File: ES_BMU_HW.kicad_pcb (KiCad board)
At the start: 2 copper layers, 100 x 100 mm, 84 parts, among them IC1 ADBMS6821CCSZ, J5 Conn_02x03_Top_Bottom, Q1 SQ2362CES, Q3 SQ2362CES, Q6 SQ2362CES, Q7 SQ2362CES, Q8 SQ2362CES, SW1 SW_Nidec_CAS-120A1, SW3 SW_Nidec_CAS-120A1, T1 74941301, U1 TPS542025, U15 SN65HVD234, U2 LM393, U3 STM32G474CETx, U4 SN65HVD234, U5 ADS1113IDGS, U7 TLV777, Y2 16 MHz

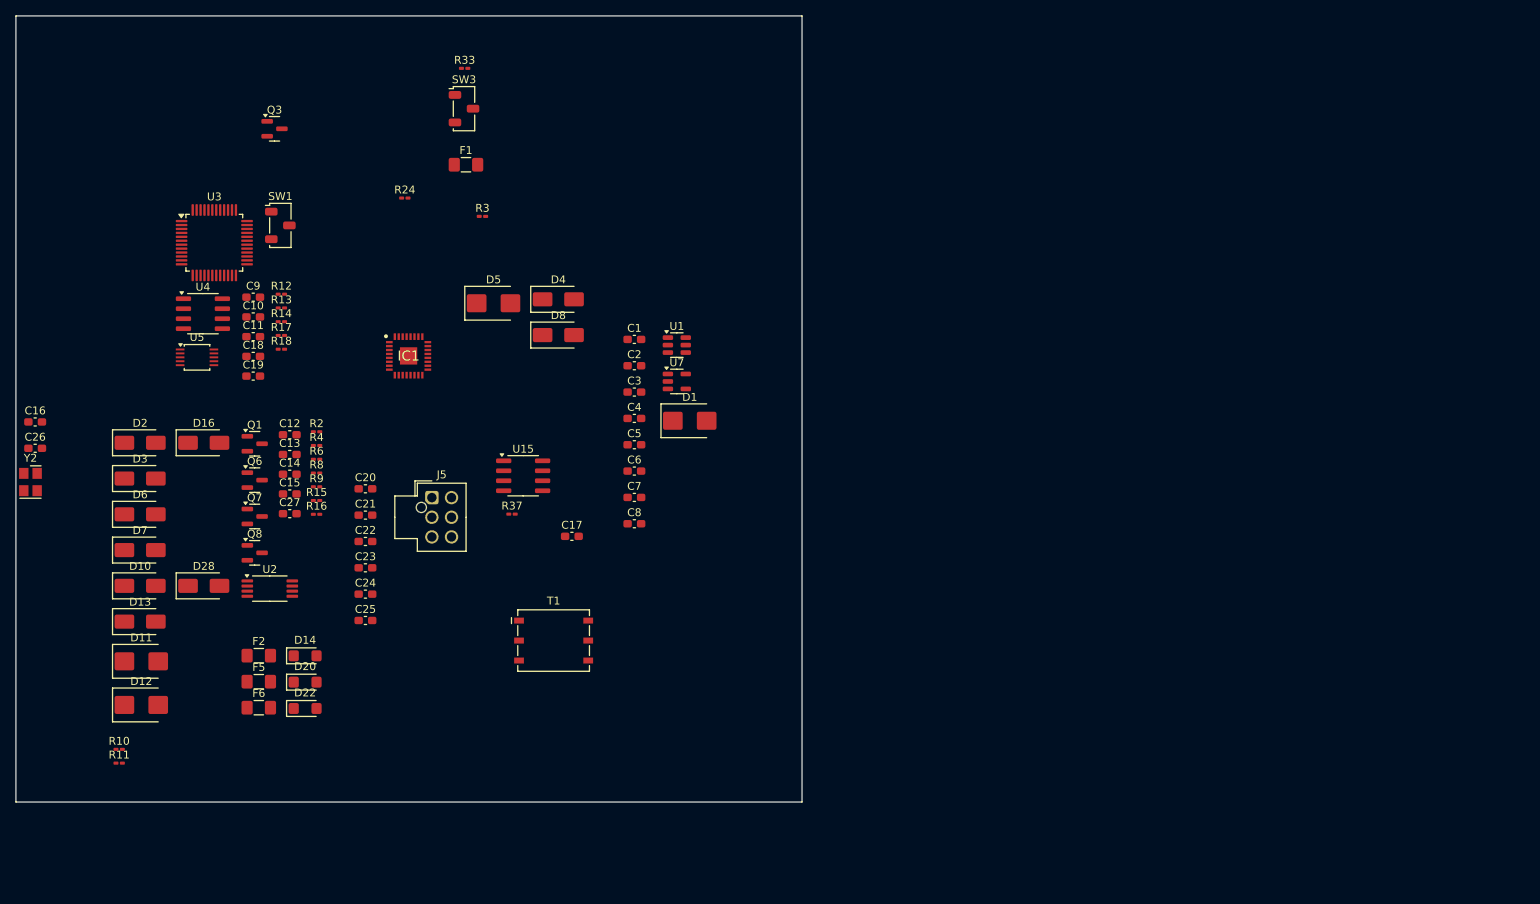
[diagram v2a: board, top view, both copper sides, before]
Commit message: - Primer placement dels components - Footprint afegit per la bobina - S'han tret els TVS a les entrades dels contactors auxiliars
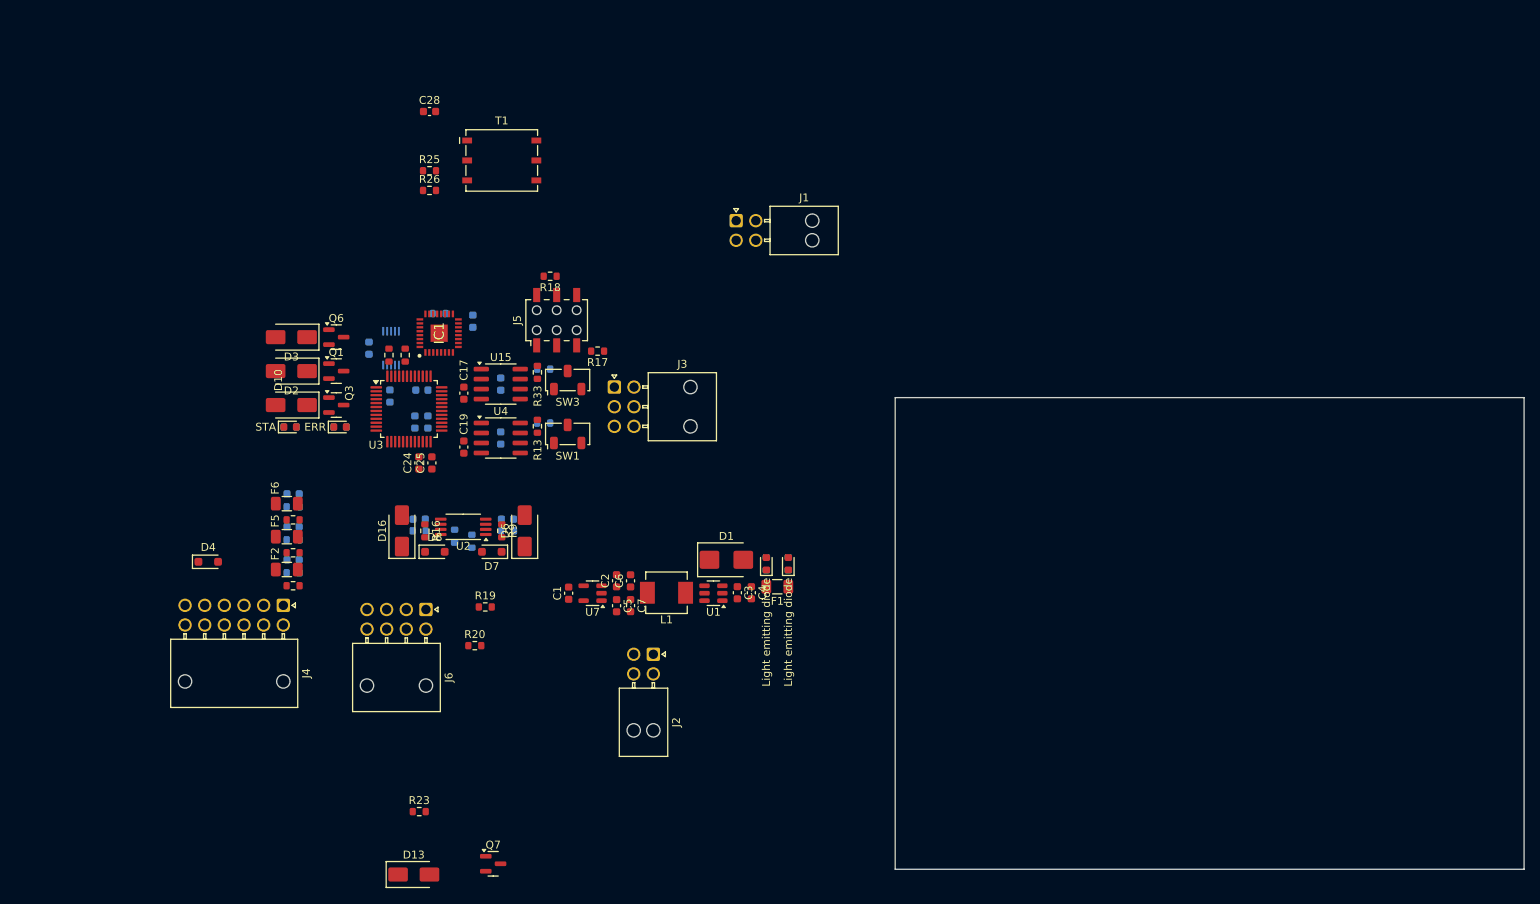
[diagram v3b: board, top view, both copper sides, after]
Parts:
- removed C16, C26: 22p, Capacitor_SMD:C_0603_1608Metric_Pad1.08x0.95mm_HandSolder
- removed D11, D12, D5: SMBJ3V3, Diode_SMD:D_SMB
- removed D20, D22: AR1FJ, Diode_SMD:D_SMF
- removed D28: SMAJ30A, Diode_SMD:D_SMA
- removed Q8: SQ2362CES, Package_TO_SOT_SMD:SOT-23
- removed R10, R11: 2k2, Resistor_SMD:R_0201_0603Metric_Pad0.64x0.40mm_HandSolder
- removed Y2: 16 MHz, Crystal_SMD_Wurth:Y_Wurth_WE-XTAL_Quartz-CFPX-180
- added C28: 1u, Capacitor_SMD:C_0603_1608Metric, F.Cu at (116.4, 51.6)
- added D15: LED, LED_SMD:LED_0603_1608Metric, F.Cu at (162.1, 109.1)
- added D17: LED, LED_SMD:LED_0603_1608Metric, F.Cu at (159.3, 109.1)
- added D9: LED, LED_SMD:LED_0603_1608Metric, F.Cu at (105.0, 91.7)
- added J1: Conn_02x02_Counter_Clockwise, Connector_Molex:Molex_Nano-Fit_105314-xx04_2x02_P2.50mm_Horizontal, F.Cu at (155.4, 65.4)
- added J2: Conn_02x02_Counter_Clockwise, Connector_Molex:Molex_Nano-Fit_105314-xx04_2x02_P2.50mm_Horizontal, F.Cu at (144.9, 120.6)
- added J3: Conn_02x03_Top_Bottom, Connector_Molex:Molex_Nano-Fit_105314-xx06_2x03_P2.50mm_Horizontal, F.Cu at (139.9, 86.6)
- added J4: Conn_02x06_Top_Bottom, Connector_Molex:Molex_Nano-Fit_105314-xx12_2x06_P2.50mm_Horizontal, F.Cu at (97.8, 114.4)
- added J6: Conn_02x04_Top_Bottom, Connector_Molex:Molex_Nano-Fit_105314-xx08_2x04_P2.50mm_Horizontal, F.Cu at (116.0, 114.9)
- added L1: 15u, Inductor_SMD:L_Vishay_IHLP-2020, F.Cu at (146.6, 112.8)
- added R1: 100, Resistor_SMD:R_0603_1608Metric, F.Cu at (99.1, 111.9)
- added R19: 100k, Resistor_SMD:R_0603_1608Metric, F.Cu at (123.5, 114.6)
- added R20: 100k, Resistor_SMD:R_0603_1608Metric, F.Cu at (122.2, 119.5)
- added R21: 2k2, Resistor_SMD:R_0603_1608Metric, B.Cu at (105.0, 91.7)
- added R22: 2k2, Resistor_SMD:R_0603_1608Metric, B.Cu at (98.7, 91.7)
- added R23: 100k, Resistor_SMD:R_0603_1608Metric, F.Cu at (115.1, 140.6)
- added R25: 100k, Resistor_SMD:R_0603_1608Metric, F.Cu at (116.4, 59.1)
- added R26: 100k, Resistor_SMD:R_0603_1608Metric, F.Cu at (116.4, 61.6)
- added R27: 10k, Resistor_SMD:R_0603_1608Metric, F.Cu at (113.3, 82.5)
- added R28: 10k, Resistor_SMD:R_0603_1608Metric, F.Cu at (111.3, 82.5)
- added R29: 10k, Resistor_SMD:R_0603_1608Metric, B.Cu at (162.1, 109.1)
- added R30: 10k, Resistor_SMD:R_0603_1608Metric, B.Cu at (159.3, 109.1)
- added R5: 100, Resistor_SMD:R_0603_1608Metric, F.Cu at (99.1, 107.7)
- added R7: 100, Resistor_SMD:R_0603_1608Metric, F.Cu at (99.1, 103.5)
- C1, C17, C19, C2, C24, C25, C3, C4, C5, C6, C7: footprint Capacitor_SMD:C_0603_1608Metric_Pad1.08x0.95mm_HandSolder -> Capacitor_SMD:C_0603_1608Metric
- C10, C11, C18, C20, C21, C22, C23, C8, C9: footprint Capacitor_SMD:C_0603_1608Metric_Pad1.08x0.95mm_HandSolder -> Capacitor_SMD:C_0603_1608Metric; moved to B.Cu
- C12, C13, C14: value 10u -> 4u7; footprint Capacitor_SMD:C_0603_1608Metric_Pad1.08x0.95mm_HandSolder -> Capacitor_SMD:C_0603_1608Metric; moved to B.Cu
- C15, C27: value 100n -> 10n; footprint Capacitor_SMD:C_0603_1608Metric_Pad1.08x0.95mm_HandSolder -> Capacitor_SMD:C_0603_1608Metric; moved to B.Cu
- D14: value AR1FJ -> LED; footprint Diode_SMD:D_SMF -> LED_SMD:LED_0603_1608Metric
- D4, D7, D8: value D_Schottky -> SD103AWS-G3-18; footprint Diode_SMD:D_SMA -> Diode_SMD:D_SOD-323_HandSoldering
- F1, F2, F5, F6: footprint Fuse:Fuse_1206_3216Metric_Pad1.42x1.75mm_HandSolder -> Fuse:Fuse_1206_3216Metric
- J5: footprint Connector_Molex:Molex_Nano-Fit_105310-xx06_2x03_P2.50mm_Vertical -> Connector_Wuerth:Wuerth_WR-PHD_610006243021_SMD_2x03_P2.54mm_Vertical
- R12, R14, R3, R37, R4, R6: footprint Resistor_SMD:R_0201_0603Metric_Pad0.64x0.40mm_HandSolder -> Resistor_SMD:R_0603_1608Metric; moved to B.Cu
- R13, R16, R17, R18, R33, R9: footprint Resistor_SMD:R_0201_0603Metric_Pad0.64x0.40mm_HandSolder -> Resistor_SMD:R_0603_1608Metric
- R15, R8: value 470k -> 100k; footprint Resistor_SMD:R_0201_0603Metric_Pad0.64x0.40mm_HandSolder -> Resistor_SMD:R_0603_1608Metric; moved to B.Cu
- R2, R24: value 10k -> 100k; footprint Resistor_SMD:R_0201_0603Metric_Pad0.64x0.40mm_HandSolder -> Resistor_SMD:R_0603_1608Metric; moved to B.Cu
- U3: value STM32G474CETx -> STM32G474CBTx
- U5: moved to B.Cu
- moved F1 66.7 mm to (160.7, 112.0), turned to 180 degrees
- moved T1 61.4 mm to (125.6, 57.8)
- moved D4 55.7 mm to (88.3, 108.8)
- moved Q7 53.6 mm to (124.5, 147.3)
- moved R3 51.3 mm to (99.1, 110.2), turned to 180 degrees
- moved D6 49.0 mm to (128.5, 104.9), turned to 90 degrees
- moved D13 47.4 mm to (114.4, 148.6)
- moved SW1 45.2 mm to (134.0, 92.6), turned to 90 degrees
- moved D7 44.7 mm to (124.3, 107.6), turned to 180 degrees
- moved R24 43.5 mm to (119.6, 105.6), turned to 90 degrees
- moved U4 41.1 mm to (125.5, 93.1)
- moved R17 40.3 mm to (137.8, 82.0), turned to 180 degrees
- moved R33 39.8 mm to (130.1, 84.7), turned to -90 degrees
- moved SW3 37.0 mm to (134.0, 85.7), turned to 90 degrees
- moved Q3 36.0 mm to (104.6, 88.9)
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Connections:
- net /GPIO/AIR+Coil- renamed AIR+Coil-
- net /GPIO/AIR-Coil- renamed AIR-Coil-
- net /GPIO/ActiveButton renamed ActiveButton
- net /GPIO/BMSStateOutput renamed BMSerrorOutput
- net /GPIO/SDCinput renamed SDCinput
- net /stm32/CAN1H renamed CAN1H
- net /stm32/CAN1L renamed CAN1L
- net /stm32/CAN2H renamed CAN2H
- net /stm32/CAN2L renamed CAN2L
- C12 pad 1: /GPIO/AuxAIRpre -> AuxAIRpre
- C13 pad 1: /GPIO/AuxAIR- -> AuxAIR-
- C14 pad 1: /GPIO/AuxAIR+ -> AuxAIR+
- D10 pad 1: /GPIO/AIRpreCoil- -> AIRpreCoil-
- D14 pad 1: SDC -> GND
- D14 pad 2: /GPIO/AIRpreCoil- -> Net-(D14-A)
- D4 pad 1: /GPIO/PwrAuxAIR+ -> PwrAuxAIR
- F2 pad 2: /GPIO/RawAuxAIRpre -> RawAuxAIRpre
- F5 pad 2: /GPIO/RawAuxAIR- -> RawAuxAIR-
- F6 pad 2: /GPIO/RawAuxAIR+ -> RawAuxAIR+
- Q1 pad 1: /GPIO/ControlAIR- -> ControlAIR-
- Q3 pad 1: /GPIO/ControlAIRpre -> ControlAIRpre
- Q3 pad 3: /GPIO/AIRpreCoil- -> AIRpreCoil-
- Q6 pad 1: /GPIO/ControlAIR+ -> ControlAIR+
- Q7 pad 1: /GPIO/ControlBMSState -> BMSerror
- R2 pad 2: /GPIO/ActiveButtonState -> ActiveButtonState
- R24 pad 2: /GPIO/SDCendState -> SDCendState
- R3 pad 1: /GPIO/AuxAIRpre -> AuxAIRpre
- R4 pad 1: /GPIO/AuxAIR- -> AuxAIR-
- R6 pad 1: /GPIO/AuxAIR+ -> AuxAIR+
- T1 pad 1: /stm32/IPA -> isoIMA
- T1 pad 3: /stm32/IMA -> isoIPA
- T1 pad 4: /stm32/IMA_EXT -> /stm32/IPA
- T1 pad 6: /stm32/IPA_EXT -> /stm32/IMA
- U2 pad 1: /GPIO/ActiveButtonState -> ActiveButtonState
- U2 pad 7: /GPIO/SDCendState -> SDCendState
- U3 pad 10: /stm32/ControlAIRpre -> ControlAIRpre
- U3 pad 11: /stm32/ControlBMSState -> LEDBMSerror
- U3 pad 12: /stm32/ControlBMSError -> LEDBMSstate
- U3 pad 13: /stm32/AuxAIR+ -> AuxAIR+
- U3 pad 14: /stm32/AuxAIR- -> AuxAIR-
- U3 pad 15: /stm32/AuxAIRpre -> AuxAIRpre
- U3 pad 17: /stm32/SDCendState -> SDCendState
- U3 pad 18: /stm32/ActiveButtonState -> ActiveButtonState
- U3 pad 28: unconnected-(U3-PB14-Pad28) -> BMSerror
- U3 pad 30: /stm32/I2C2_SDA -> unconnected-(U3-PA8-Pad30)
- U3 pad 31: /stm32/I2C2_SCL -> unconnected-(U3-PA9-Pad31)
- U3 pad 39: unconnected-(U3-PA15-Pad39) -> /stm32/SPI1_CS
- U3 pad 45: unconnected-(U3-PB8-Pad45) -> /stm32/I2C2_SCL
- U3 pad 46: /stm32/SPI1_CS -> /stm32/I2C2_SDA
- U3 pad 5: Net-(U3-PF0) -> unconnected-(U3-PF0-Pad5)
- U3 pad 6: Net-(U3-PF1) -> unconnected-(U3-PF1-Pad6)
- U3 pad 8: /stm32/ControlAIR+ -> ControlAIR+
- U3 pad 9: /stm32/ControlAIR- -> ControlAIR-
- U5 pad 4: /stm32/HallVout -> HallVout
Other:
- board size 100 x 100 mm -> 80 x 60 mm

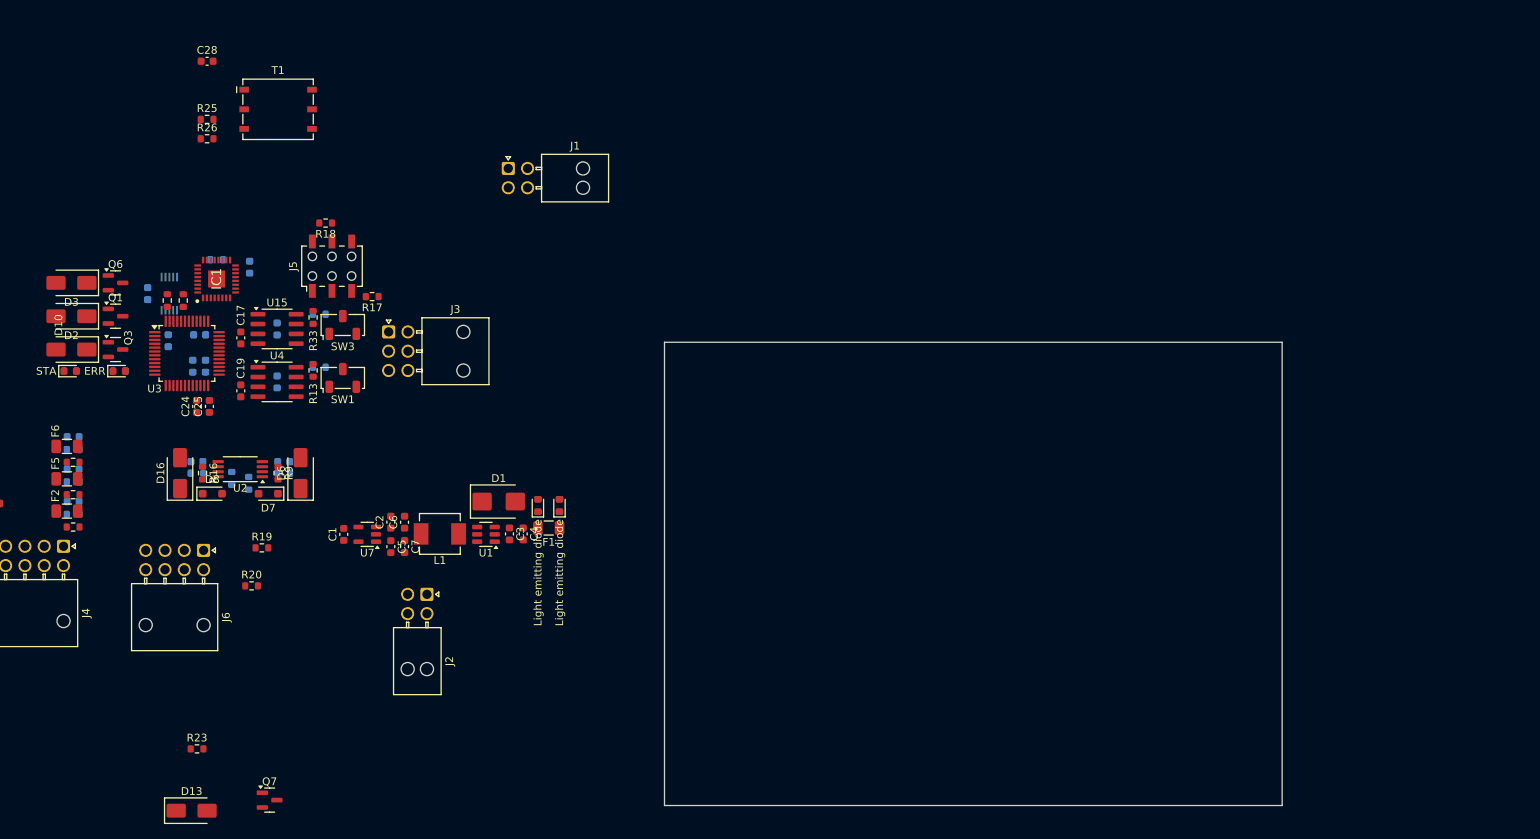
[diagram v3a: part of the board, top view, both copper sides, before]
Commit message: - S'han definit tots els parts numbers de R,C i D ajustant a voltatges i potències - Connectors 02x02 canviats a top2bottom - Modificació de l'error de BMS amb sortida open collector - LED blau afegit per saber l'estat de SDC
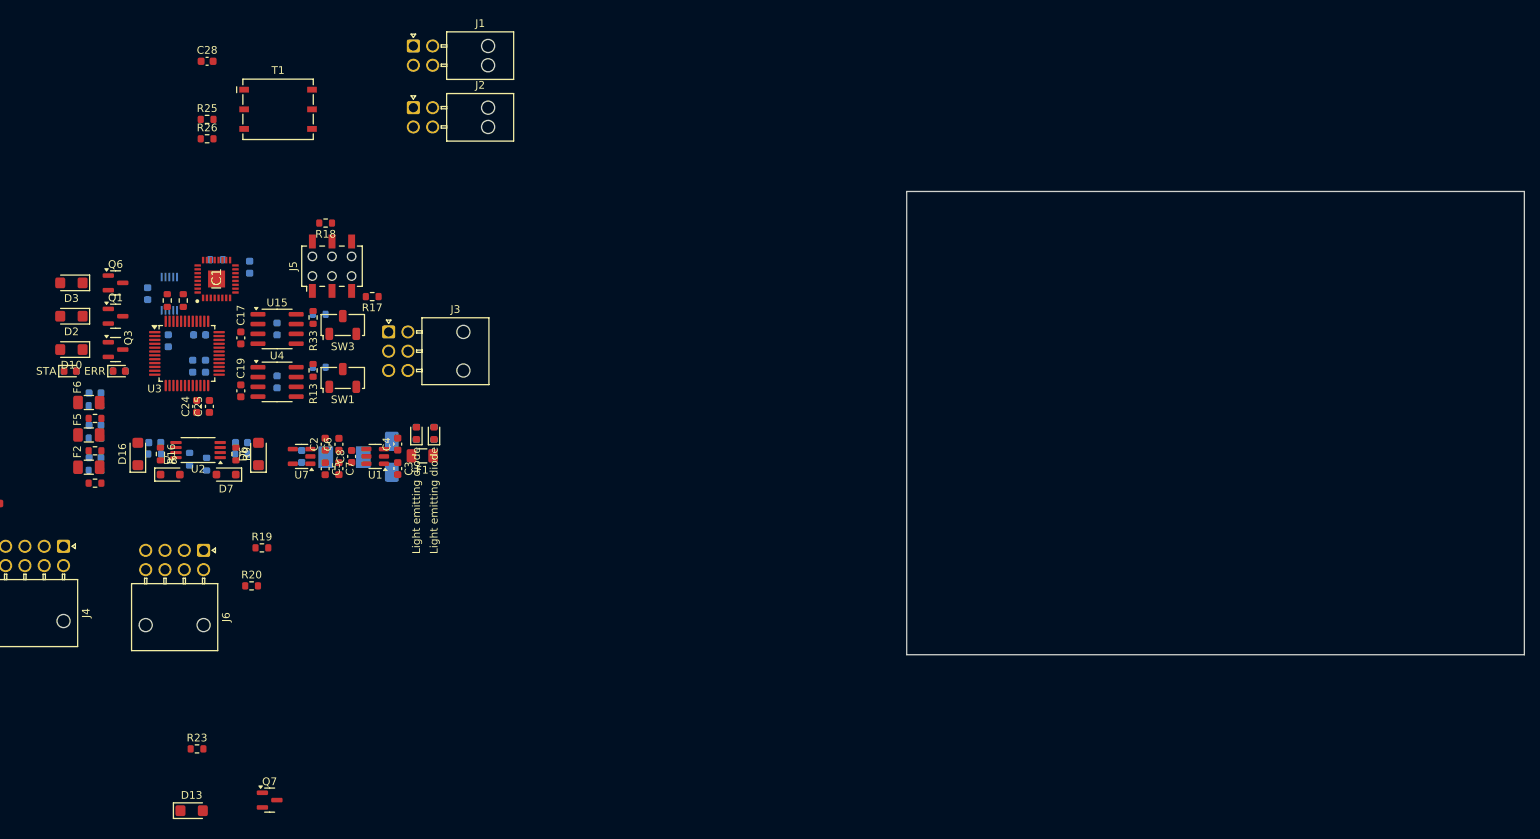
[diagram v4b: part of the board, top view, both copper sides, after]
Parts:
- C1, L1: moved to B.Cu
- C8: moved to F.Cu
- D1: value SMBJ30A -> SMAJ30A; footprint Diode_SMD:D_SMB -> Diode_SMD:D_SMA; moved to B.Cu
- D10, D13, D16, D2, D3, D6: value SMAJ30A -> SMF30A; footprint Diode_SMD:D_SMA -> Diode_SMD:D_SMF
- J1, J2: value Conn_02x02_Counter_Clockwise -> Conn_02x02_Top_Bottom
- R21, R22: value 2k2 -> 470
- R25, R26: value 100k -> 60R4
- moved J2 63.1 mm to (143.1, 57.6), turned to 0 degrees
- moved J1 20.1 mm to (143.1, 49.6)
- moved C4 20.0 mm to (141.1, 101.1), turned to 90 degrees
- moved F1 18.9 mm to (144.3, 102.7)
- moved D15 18.7 mm to (145.8, 99.7)
- moved R29 18.7 mm to (145.8, 99.7)
- moved D17 18.3 mm to (143.5, 99.7)
- moved R30 18.3 mm to (143.5, 99.7)
- moved U1 17.5 mm to (138.2, 102.7)
- moved C8 17.1 mm to (135.1, 102.7)
- moved C3 16.8 mm to (141.1, 104.3)
- moved L1 15.8 mm to (134.2, 102.8)
- moved D1 15.0 mm to (140.3, 102.8), turned to -90 degrees
- moved C5 13.2 mm to (131.7, 104.3)
- moved C7 13.2 mm to (133.5, 104.3)
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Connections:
- D1 pad 1: GND -> +24V
- D1 pad 2: +24V -> GND
- J1 pad 3: unconnected-(J1-Pin_3-Pad3) -> isoIMA
- J1 pad 4: isoIMA -> unconnected-(J1-Pin_4-Pad4)
- J2 pad 3: GND -> unconnected-(J2-Pin_3-Pad3)
- J2 pad 4: unconnected-(J2-Pin_4-Pad4) -> GND
